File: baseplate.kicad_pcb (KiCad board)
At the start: 2 copper layers, 35.7 x 32 mm, 13 parts, among them J1 10144042-04011LF, M1 THRU_HOLE_PAD, M2 THRU_HOLE_PAD, M3 THRU_HOLE_PAD, M4 THRU_HOLE_PAD, M5 THRU_HOLE_PAD, M6 THRU_HOLE_PAD, M7 THRU_HOLE_PAD, U1 STM32L011F4Ux

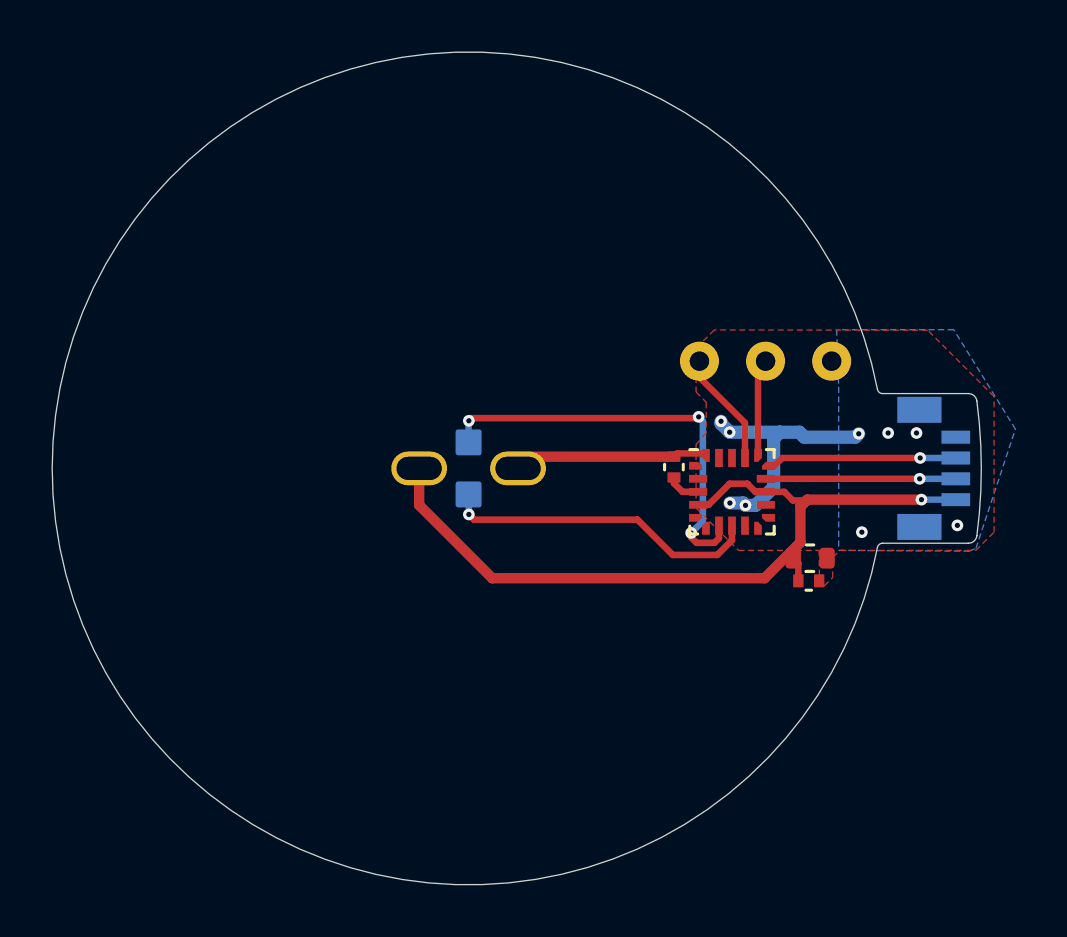
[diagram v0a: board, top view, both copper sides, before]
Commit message: mounting holes
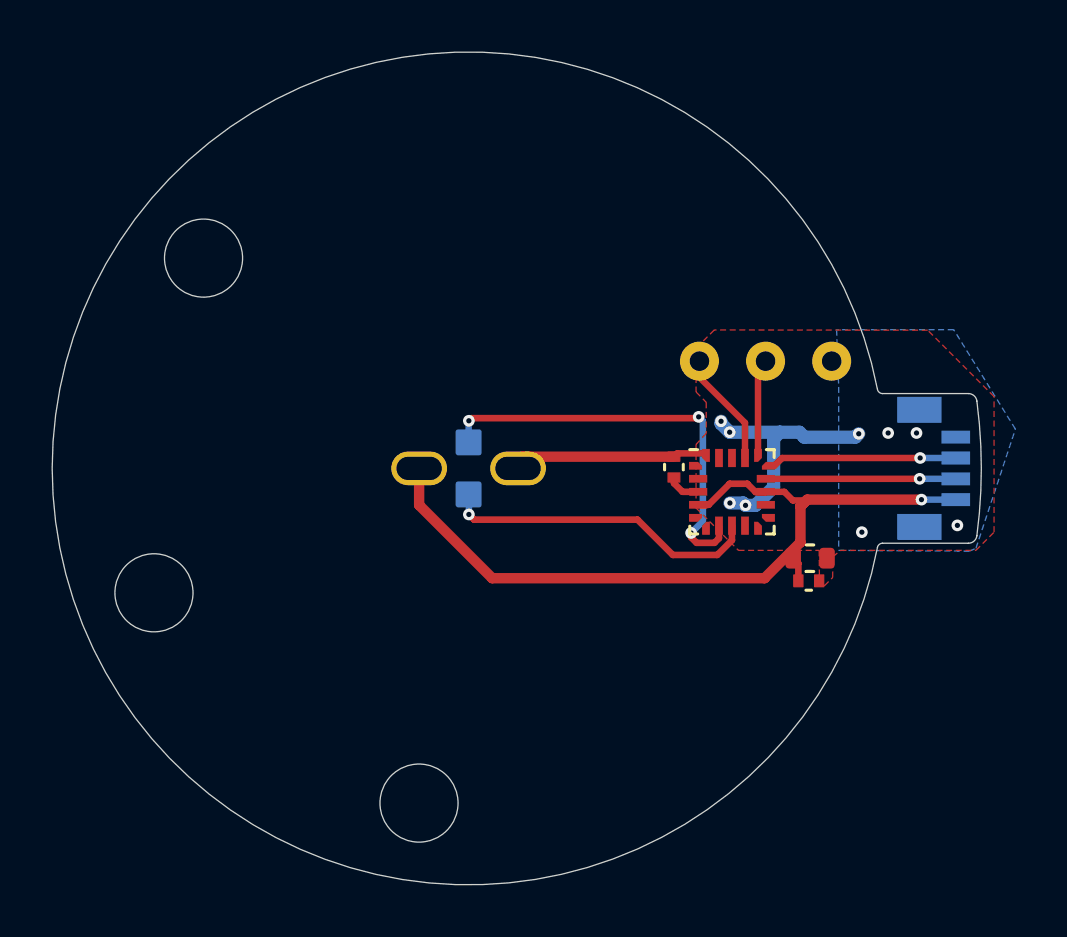
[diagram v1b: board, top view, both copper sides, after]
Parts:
- added M10: THRU_HOLE_PAD, adapter-encoder:MountingHole3mm, F.Cu at (141.5, 115.0)
- added M8: THRU_HOLE_PAD, adapter-encoder:MountingHole3mm, F.Cu at (133.2, 94.0)
- added M9: THRU_HOLE_PAD, adapter-encoder:MountingHole3mm, F.Cu at (131.3, 106.9)
- renumbered M1 to M100000
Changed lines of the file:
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@@
   (net 17 "unconnected-(U1-PB7-Pad19)")
   (net 18 "+3V3")
+  (footprint "adapter-encoder:MountingHole3mm" locked (layer "F.Cu")
+    (at 141.509772 114.959631)
+    (property "Sheetfile" "baseplate.kicad_sch")
+    (property "Sheetname" "")
+    (property "exclude_from_bom" "")
+    (attr exclude_from_bom)
+    (fp_text reference "M10" (at 0 -2.1) (layer "F.SilkS") hide
+        (effects (font (size 1.27 1.27) (thickness 0.15)))
+    )
+    (fp_text value "THRU_HOLE_PAD" (at 0.1 -2.1) (layer "F.SilkS") hide
+        (effects (font (size 1.27 1.27) (thickness 0.15)))
+    )
+    (pad "" np_thru_hole oval locked (at 0 0) (size 3 3) (drill 3) (layers "*.Mask")
+      (thermal_bridge_angle 45))
+  )
   (footprint "adapter-encoder:dogbone_slot" (layer "F.Cu")
     (at 143.415 102.1)
@@
     (property "exclude_from_bom" "")
     (attr smd board_only exclude_from_bom)
-    (fp_text reference "M1" (at 0 -1.4 unlocked) (layer "F.SilkS") hide
+    (fp_text reference "M100000" (at 0 -1.4 unlocked) (layer "F.SilkS") hide
         (effects (font (size 1 1) (thickness 0.15)))
     )
@@
     (pad "1" thru_hole oval locked (at 0 0) (size 2.15 1.3) (drill oval 1.75 0.9) (layers "*.Cu" "*.Mask")
       (net 18 "+3V3") (pinfunction "1") (pintype "passive") (thermal_bridge_angle 45))
+  )
+  (footprint "adapter-encoder:MountingHole3mm" locked (layer "F.Cu")
+    (at 133.230847 94.02021)
+    (property "Sheetfile" "baseplate.kicad_sch")
+    (property "Sheetname" "")
+    (property "exclude_from_bom" "")
+    (attr exclude_from_bom)
+    (fp_text reference "M8" (at 0 -2.1) (layer "F.SilkS") hide
+        (effects (font (size 1.27 1.27) (thickness 0.15)))
+    )
+    (fp_text value "THRU_HOLE_PAD" (at 0.1 -2.1) (layer "F.SilkS") hide
+        (effects (font (size 1.27 1.27) (thickness 0.15)))
+    )
+    (pad "" np_thru_hole oval locked (at 0 0) (size 3 3) (drill 3) (layers "*.Mask")
+      (thermal_bridge_angle 45))
   )
   (footprint "adapter-encoder:dogbone_slot" locked (layer "F.Cu")
@@
     )
   )
+  (footprint "adapter-encoder:MountingHole3mm" locked (layer "F.Cu")
+    (at 131.325619 106.87984)
+    (property "Sheetfile" "baseplate.kicad_sch")
+    (property "Sheetname" "")
+    (property "exclude_from_bom" "")
+    (attr exclude_from_bom)
+    (fp_text reference "M9" (at 0 -2.1) (layer "F.SilkS") hide
+        (effects (font (size 1.27 1.27) (thickness 0.15)))
+    )
+    (fp_text value "THRU_HOLE_PAD" (at 0.1 -2.1) (layer "F.SilkS") hide
+        (effects (font (size 1.27 1.27) (thickness 0.15)))
+    )
+    (pad "" np_thru_hole oval locked (at 0 0) (size 3 3) (drill 3) (layers "*.Mask")
+      (thermal_bridge_angle 45))
+  )
   (footprint "adapter-encoder:dogbone_pad" locked (layer "B.Cu")
